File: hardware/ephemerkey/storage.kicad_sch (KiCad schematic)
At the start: 2 parts, among them U7 M24M02E

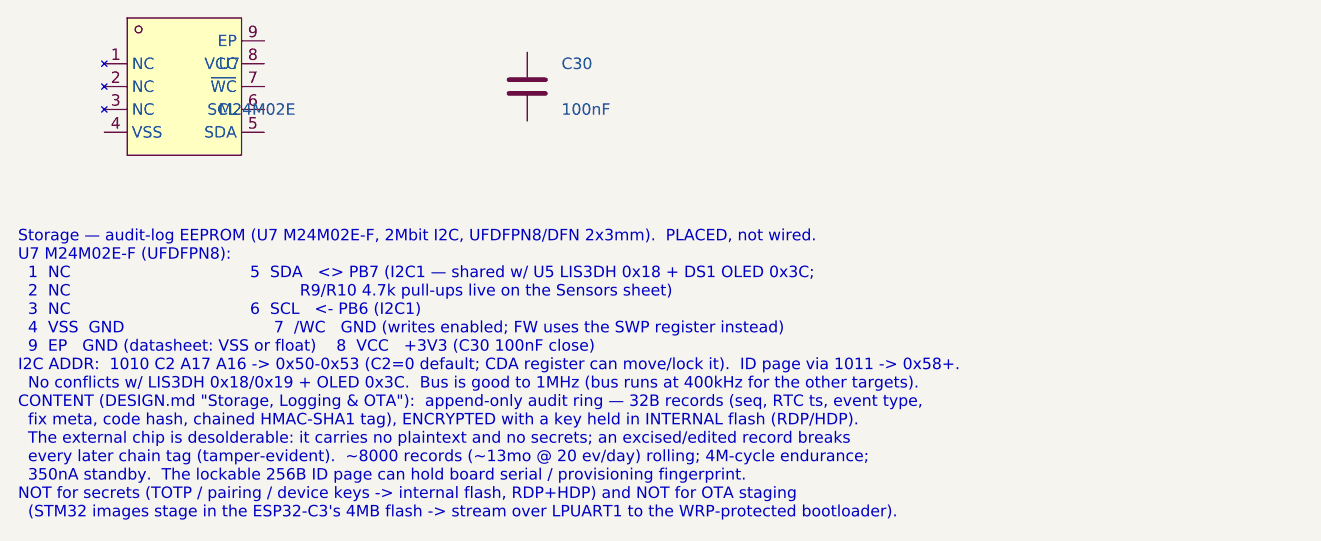
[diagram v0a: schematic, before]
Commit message: hardware: gate OLED/EEPROM/I2C1 pull-ups behind PERI_EN load switch
Free the LIS3DH 2nd interrupt pin (tamper/free-fall now OR'd onto INT1 via
CTRL_REG3 I1_IA2) and repurpose it as PERI_EN. Add a high-side load switch on
the Sensors sheet (Q3 AO3401A pass FET, Q4 AO3400A gate driver, R30/R31 100k,
C31 1uF) powering a new +3V3_SW rail for DS1 OLED, U7 EEPROM, and the I2C1
pull-ups R9/R10 -- all gated off in Stop so they don't leak. LIS3DH stays on
always-on +3V3 as the wake source; FW drives PB6/PB7 low before Stop so the
powered accel never floats on the unpulled bus.

Surgical edits to both the .kicad_sch sheets and the schgen manifests (no
regen -- sheets are already partially wired). PARTS.md updated (also fills the
previously-missing Q2 AO3400A row). Also fix the lock J2 note: pin 2 = VCC <-
ephemerkey VSYS (was mislabeled "No-Connect", contradicting the wired net).

Co-Authored-By: Claude Opus 4.8 (1M context) <noreply@anthropic.com>
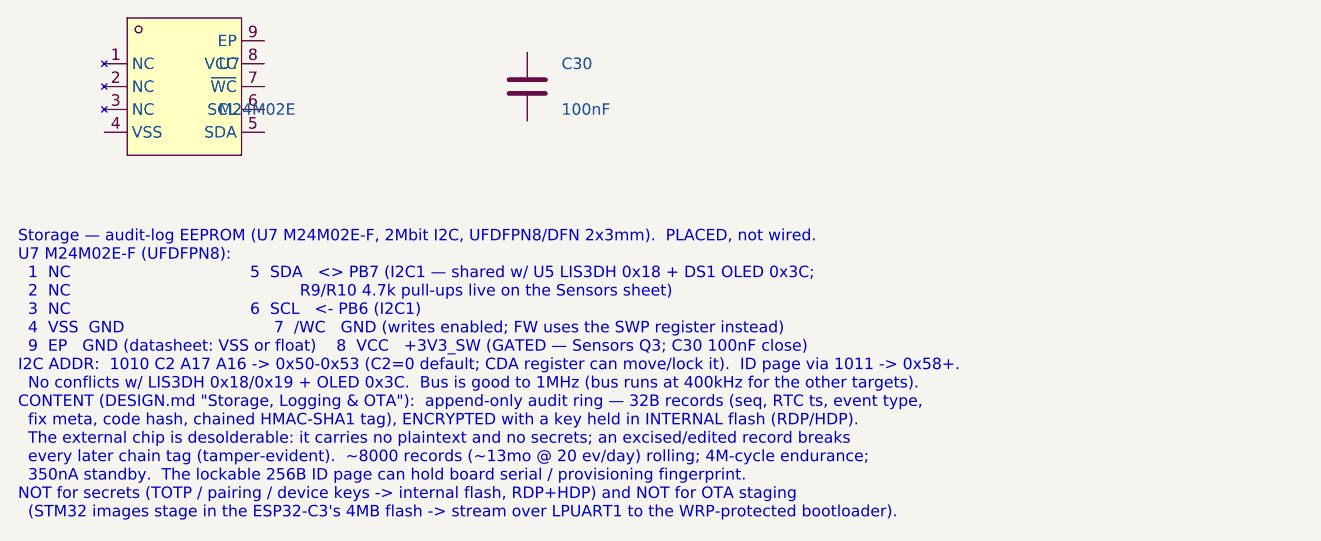
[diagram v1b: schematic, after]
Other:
- note added: "Storage — audit-log EEPROM (U7 M24M02E-F, 2Mbit I2C, UFDFPN8/DFN 2x3mm). PLACED, not wired. U7 M24M02E-F (UFDFPN8): 1 NC 5 SDA <> PB7 (I2C1 — shared w/ U5 LIS3DH 0x18 + DS1 OLED 0x3C; 2 NC R9/R10 4.7k pull-ups live on the Sensors sheet) 3 NC 6 SCL <- PB6 (I2C1) 4 VSS GND 7 /WC GND (writes enabled; FW uses the SWP register instead) 9 EP GND (datasheet: VSS or float) 8 VCC +3V3_SW (GATED — Sensors 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"
- note removed: "Storage — audit-log EEPROM (U7 M24M02E-F, 2Mbit I2C, UFDFPN8/DFN 2x3mm). PLACED, not wired. U7 M24M02E-F (UFDFPN8): 1 NC 5 SDA <> PB7 (I2C1 — shared w/ U5 LIS3DH 0x18 + DS1 OLED 0x3C; 2 NC R9/R10 4.7k pull-ups live on the Sensors sheet) 3 NC 6 SCL <- PB6 (I2C1) 4 VSS GND 7 /WC GND (writes enabled; FW uses the SWP register instead) 9 EP GND (datasheet: VSS or float) 8 VCC +3V3 (C30 100nF close) I2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"
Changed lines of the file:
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@@
 		)
 	)
-	(text "Storage — audit-log EEPROM (U7 M24M02E-F, 2Mbit I2C, UFDFPN8/DFN 2x3mm).  PLACED, not wired.\nU7 M24M02E-F (UFDFPN8):\n  1  NC                                    5  SDA   <> PB7 (I2C1 — shared w/ U5 LIS3DH 0x18 + DS1 OLED 0x3C;\n  2  NC                                              R9/R10 4.7k pull-ups live on the Sensors sheet)\n  3  NC                                    6  SCL   <- PB6 (I2C1)\n  4  VSS  GND                              7  /WC   GND (writes enabled; FW uses the SWP register instead)\n  9  EP   GND (datasheet: VSS or float)    8  VCC   +3V3 (C30 100nF close)\nI2C ADDR:  1010 C2 A17 A16 -> 0x50-0x53 (C2=0 default; CDA register can move/lock it).  ID page via 1011 -> 0x58+.\n  No conflicts w/ LIS3DH 0x18/0x19 + OLED 0x3C.  Bus is good to 1MHz (bus runs at 400kHz for the other targets).\nCONTENT (DESIGN.md \"Storage, Logging & OTA\"):  append-only audit ring — 32B records (seq, RTC ts, event type,\n  fix meta, code hash, chained HMAC-SHA1 tag), ENCRYPTED with a key held in INTERNAL flash (RDP/HDP).\n  The external chip is desolderable: it carries no plaintext and no secrets; an excised/edited record breaks\n  every later chain tag (tamper-evident).  ~8000 records (~13mo @ 20 ev/day) rolling; 4M-cycle endurance;\n  350nA standby.  The lockable 256B ID page can hold board serial / provisioning fingerprint.\nNOT for secrets (TOTP / pairing / device keys -> internal flash, RDP+HDP) and NOT for OTA staging\n  (STM32 images stage in the ESP32-C3's 4MB flash -> stream over LPUART1 to the WRP-protected bootloader)."
+	(text "Storage — audit-log EEPROM (U7 M24M02E-F, 2Mbit I2C, UFDFPN8/DFN 2x3mm).  PLACED, not wired.\nU7 M24M02E-F (UFDFPN8):\n  1  NC                                    5  SDA   <> PB7 (I2C1 — shared w/ U5 LIS3DH 0x18 + DS1 OLED 0x3C;\n  2  NC                                              R9/R10 4.7k pull-ups live on the Sensors sheet)\n  3  NC                                    6  SCL   <- PB6 (I2C1)\n  4  VSS  GND                              7  /WC   GND (writes enabled; FW uses the SWP register instead)\n  9  EP   GND (datasheet: VSS or float)    8  VCC   +3V3_SW (GATED — Sensors Q3; C30 100nF close)\nI2C ADDR:  1010 C2 A17 A16 -> 0x50-0x53 (C2=0 default; CDA register can move/lock it).  ID page via 1011 -> 0x58+.\n  No conflicts w/ LIS3DH 0x18/0x19 + OLED 0x3C.  Bus is good to 1MHz (bus runs at 400kHz for the other targets).\nCONTENT (DESIGN.md \"Storage, Logging & OTA\"):  append-only audit ring — 32B records (seq, RTC ts, event type,\n  fix meta, code hash, chained HMAC-SHA1 tag), ENCRYPTED with a key held in INTERNAL flash (RDP/HDP).\n  The external chip is desolderable: it carries no plaintext and no secrets; an excised/edited record breaks\n  every later chain tag (tamper-evident).  ~8000 records (~13mo @ 20 ev/day) rolling; 4M-cycle endurance;\n  350nA standby.  The lockable 256B ID page can hold board serial / provisioning fingerprint.\nNOT for secrets (TOTP / pairing / device keys -> internal flash, RDP+HDP) and NOT for OTA staging\n  (STM32 images stage in the ESP32-C3's 4MB flash -> stream over LPUART1 to the WRP-protected bootloader)."
 		(exclude_from_sim no)
 		(at 12.00 56.64 0)
